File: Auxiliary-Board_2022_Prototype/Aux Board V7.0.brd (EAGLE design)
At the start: 114.3 x 96.6 mm, 56 parts, among them CON11 1X01, CON12 1X01, CON13 1X01, CON14 1X01, CON15 1X01, CON16 1X01, CON17 1X01, CON18 1X01, CON5 1X01, CON8 1X01, IC1 RS232-TTL_MAX232E

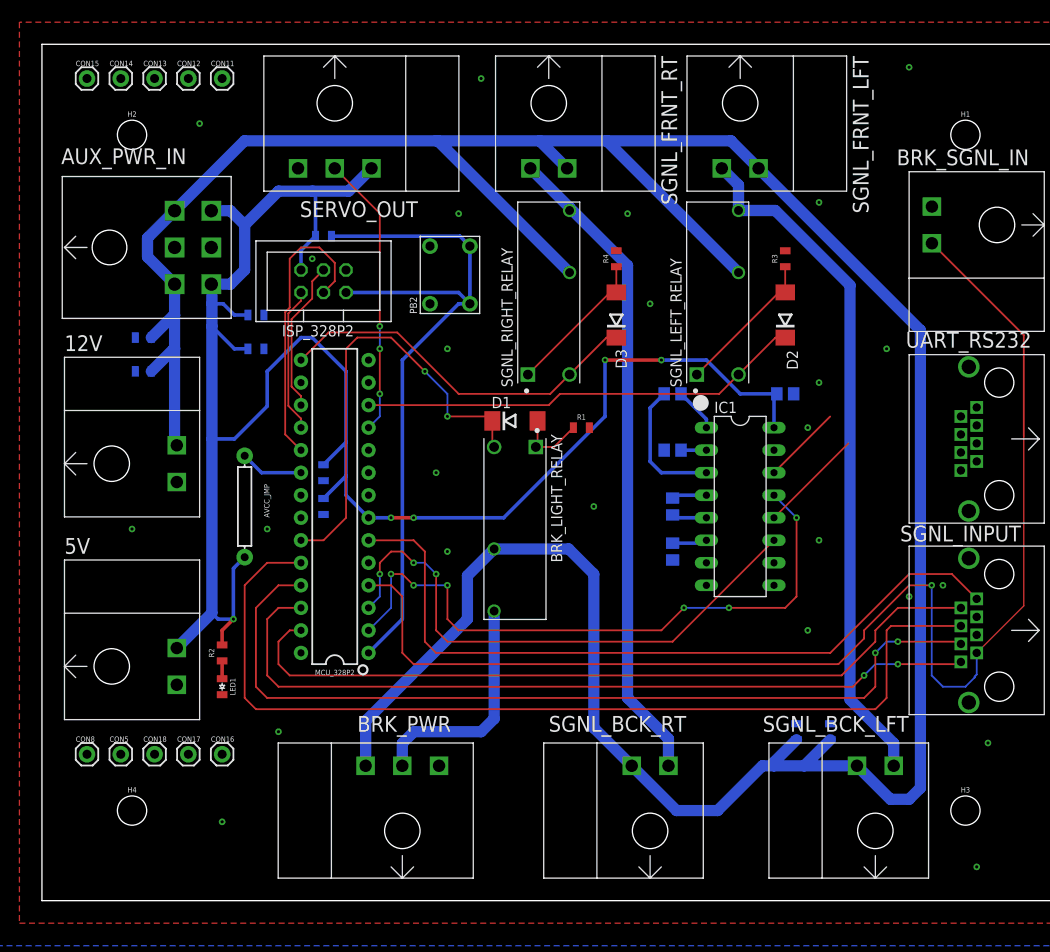
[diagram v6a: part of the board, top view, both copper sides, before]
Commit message: feat: add EcoCar logo and version on board
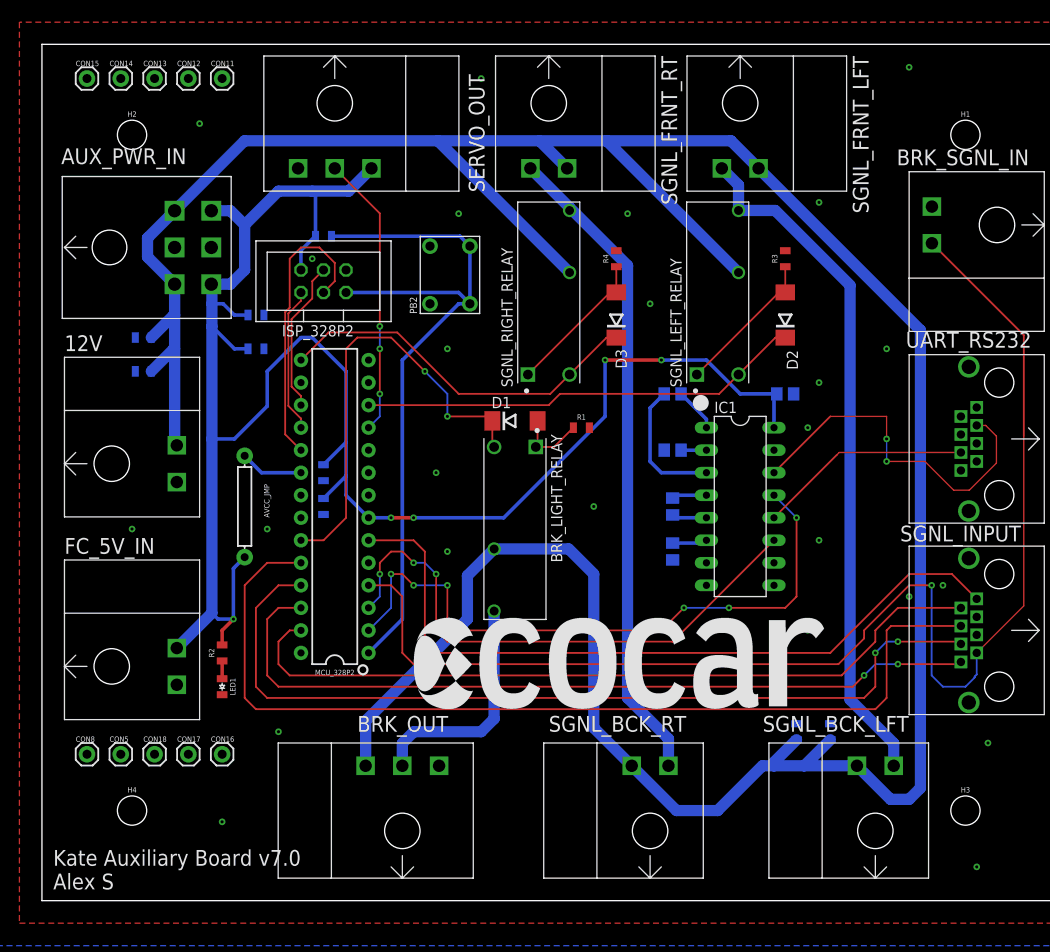
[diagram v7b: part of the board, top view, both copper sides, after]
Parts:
- added U$1: (no value), EcoCar-Miscellaneous:ECOCAR_LOGO_2018
- renumbered 5V to FC_5V_IN, BRK_PWR to BRK_OUT
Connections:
- net RS_RX: now also UART_RS232.6; no longer UART_RS232.3
- net RS_TX: now also UART_RS232.3; no longer UART_RS232.6
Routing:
- net RS_TX: track 8.97 -> 41.2 mm, vias 0 -> 2
- net RS_RX: track 11.9 -> 24.1 mm
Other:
- board text added: "Kate Auxiliary Board v7.0 Alex S"
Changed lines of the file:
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@@
 <wire x1="114.28" y1="101.651" x2="0" y2="101.651" width="0" layer="20"/>
 <wire x1="0" y1="101.651" x2="0" y2="5.08" width="0" layer="20"/>
+<text x="1.27" y="6.35" size="1.778" layer="25">Kate Auxiliary Board v7.0
+Alex S</text>
 </plain>
 <attributes>
@@
 <attribute name="NAME" x="2.54" y="67.056" size="1.778" layer="25"/>
 </element>
-<element name="5V" library="EcoCar-Connectors" package="TE_2-PIN" value="TE_2-PIN" x="2.54" y="31.496" smashed="yes" rot="R270">
+<element name="FC_5V_IN" library="EcoCar-Connectors" package="TE_2-PIN" value="TE_2-PIN" x="2.54" y="31.496" smashed="yes" rot="R270">
 <attribute name="NAME" x="2.54" y="44.196" size="1.778" layer="25"/>
 </element>
@@
 <attribute name="VALUE" x="48.124459375" y="57.6755" size="1.27208125" layer="27" rot="R270"/>
 </element>
-<element name="BRK_PWR" library="EcoCar-Connectors" package="TE_3-PIN" value="TE_3-PIN" x="40.64" y="7.62" smashed="yes">
+<element name="BRK_OUT" library="EcoCar-Connectors" package="TE_3-PIN" value="TE_3-PIN" x="40.64" y="7.62" smashed="yes">
 <attribute name="NAME" x="35.56" y="24.13" size="1.778" layer="25"/>
 </element>
@@
 </element>
 <element name="SERVO_OUT" library="EcoCar-Connectors" package="TE_3-PIN" value="TE_3-PIN" x="33.02" y="100.33" smashed="yes" rot="R180">
-<attribute name="NAME" x="29.083" y="82.169" size="1.778" layer="25"/>
+<attribute name="NAME" x="49.911" y="84.963" size="1.778" layer="25" rot="R90"/>
 </element>
 <element name="SGNL_BCK_LFT" library="EcoCar-Connectors" package="TE_2-PIN" value="TE_2-PIN" x="93.98" y="7.62" smashed="yes">
@@
 <attribute name="VALUE" x="67.476" y="68.48" size="1.27" layer="27" ratio="10" rot="R90"/>
 </element>
+<element name="U$1" library="EcoCar-Miscellaneous" package="ECOCAR_LOGO_2018" value="" x="41.91" y="26.67" smashed="yes"/>
 </elements>
 <signals>
@@
 <contactref element="SGNL_INPUT" pad="9"/>
 <contactref element="SGNL_INPUT" pad="10"/>
-<contactref element="5V" pad="2"/>
+<contactref element="FC_5V_IN" pad="2"/>
 <contactref element="12V" pad="2"/>
-<contactref element="BRK_PWR" pad="3"/>
+<contactref element="BRK_OUT" pad="3"/>
 <contactref element="SERVO_OUT" pad="3"/>
 <contactref element="C1" pad="1"/>
@@
 <contactref element="UART_RS232" pad="4"/>
 <contactref element="UART_RS232" pad="5"/>
-<wire x1="83.82" y1="78.37" x2="100.36" y2="83.35" width="0" layer="19" extent="1-1"/>
-<wire x1="87.63" y1="63.5" x2="83.82" y2="78.37" width="0" layer="19" extent="1-1"/>
-<wire x1="84.77" y1="62.23" x2="87.63" y2="63.5" width="0" layer="19" extent="16-16"/>
-<wire x1="82.55" y1="55.88" x2="84.77" y2="62.23" width="0" layer="19" extent="16-16"/>
-<wire x1="70.17" y1="55.88" x2="82.55" y2="55.88" width="0" layer="19" extent="16-16"/>
-<wire x1="61.733" y1="58.42" x2="70.17" y2="55.88" width="0" layer="19" extent="1-16"/>
-<wire x1="71.12" y1="43.5" x2="70.17" y2="55.88" width="0" layer="19" extent="16-16"/>
-<wire x1="68.58" y1="72.39" x2="61.733" y2="58.42" width="0" layer="19" extent="1-1"/>
-<wire x1="64.77" y1="78.37" x2="68.58" y2="72.39" width="0" layer="19" extent="1-1"/>
-<wire x1="104.52" y1="65.28" x2="87.63" y2="63.5" width="0" layer="19" extent="1-1"/>
-<wire x1="103.63" y1="57.65" x2="104.52" y2="65.28" width="0" layer="19" extent="1-1"/>
-<wire x1="105.41" y1="56.64" x2="103.63" y2="57.65" width="0" layer="19" extent="1-1"/>
-<wire x1="104.52" y1="49.02" x2="105.41" y2="56.64" width="0" layer="19" extent="1-1"/>
-<wire x1="104.52" y1="43.69" x2="104.52" y2="49.02" width="0" layer="19" extent="1-1"/>
-<wire x1="101.6" y1="40.64" x2="104.52" y2="43.69" width="0" layer="19" extent="1-1"/>
-<wire x1="97.79" y1="39.37" x2="101.6" y2="40.64" width="0" layer="19" extent="1-1"/>
-<wire x1="105.41" y1="37.08" x2="101.6" y2="40.64" width="0" layer="19" extent="1-1"/>
-<wire x1="105.41" y1="35.05" x2="105.41" y2="37.08" width="0" layer="19" extent="1-1"/>
-<wire x1="104.52" y1="27.43" x2="105.41" y2="35.05" width="0" layer="19" extent="1-1"/>
-<wire x1="86.36" y1="35.56" x2="97.79" y2="39.37" width="0" layer="19" extent="1-1"/>
-<wire x1="85.09" y1="25.03" x2="86.36" y2="35.56" width="0" layer="19" extent="16-16"/>
-<wire x1="88.9" y1="25.03" x2="85.09" y2="25.03" width="0" layer="19" extent="16-16"/>
-<wire x1="45.72" y1="67.31" x2="61.733" y2="58.42" width="0" layer="19" extent="1-1"/>
-<wire x1="43.76" y1="72.39" x2="45.72" y2="67.31" width="0" layer="19" extent="1-1"/>
-<wire x1="43.76" y1="78.89" x2="43.76" y2="72.39" width="0" layer="19" extent="1-1"/>
-<wire x1="34.29" y1="76.2" x2="43.76" y2="78.89" width="0" layer="19" extent="1-1"/>
-<wire x1="30.48" y1="77.47" x2="34.29" y2="76.2" width="0" layer="19" extent="1-1"/>
-<wire x1="25.03" y1="71.12" x2="30.48" y2="77.47" width="0" layer="19" extent="16-16"/>
-<wire x1="25.03" y1="67.31" x2="25.03" y2="71.12" width="0" layer="19" extent="16-16"/>
-<wire x1="19.1" y1="78.74" x2="25.03" y2="71.12" width="0" layer="19" extent="16-16"/>
-<wire x1="14.96" y1="78.74" x2="19.1" y2="78.74" width="0" layer="19" extent="1-1"/>
-<wire x1="28.88" y1="87.66" x2="30.48" y2="77.47" width="0" layer="19" extent="1-1"/>
-<wire x1="10.53" y1="68.58" x2="14.96" y2="78.74" width="0" layer="19" extent="16-16"/>
-<wire x1="10.53" y1="64.77" x2="10.53" y2="68.58" width="0" layer="19" extent="16-16"/>
-<wire x1="15.21" y1="52.286" x2="10.53" y2="64.77" width="0" layer="19" extent="16-16"/>
-<wire x1="25.4" y1="46.99" x2="15.21" y2="52.286" width="0" layer="19" extent="1-1"/>
-<wire x1="29.21" y1="48.26" x2="25.4" y2="46.99" width="0" layer="19" extent="1-1"/>
-<wire x1="31.75" y1="48.63" x2="29.21" y2="48.26" width="0" layer="19" extent="16-16"/>
-<wire x1="31.75" y1="52.44" x2="31.75" y2="48.63" width="0" layer="19" extent="16-16"/>
-<wire x1="36.83" y1="50.8" x2="31.75" y2="52.44" width="0" layer="19" extent="16-16"/>
-<wire x1="20.32" y1="28.31" x2="25.4" y2="46.99" width="0" layer="19" extent="1-1"/>
-<wire x1="15.21" y1="29.426" x2="20.32" y2="28.31" width="0" layer="19" extent="1-1"/>
-<wire x1="26.67" y1="24.13" x2="20.32" y2="28.31" width="0" layer="19" extent="1-1"/>
-<wire x1="44.78" y1="20.29" x2="26.67" y2="24.13" width="0" layer="19" extent="1-1"/>
 </signal>
 <signal name="12V">
@@
 <contactref element="C7" pad="2"/>
 <contactref element="C5" pad="2"/>
-<contactref element="BRK_PWR" pad="1"/>
+<contactref element="BRK_OUT" pad="1"/>
 <contactref element="AUX_PWR_IN" pad="4"/>
 <contactref element="AUX_PWR_IN" pad="6"/>
@@
 <wire x1="95.69" y1="16.51" x2="91.91" y2="20.29" width="1.27" layer="16"/>
 <wire x1="99.06" y1="69.41" x2="99.06" y2="17.78" width="1.27" layer="16"/>
-<wire x1="22.8474" y1="90.7674" x2="44.45" y2="90.7674" width="1.27" layer="16"/>
+<wire x1="22.8474" y1="90.7674" x2="44.6426" y2="90.7674" width="1.27" layer="16"/>
 <wire x1="44.6426" y1="90.7674" x2="56.1126" y2="90.7674" width="1.27" layer="16"/>
 <wire x1="59.22" y1="87.66" x2="56.1126" y2="90.7674" width="1.27" layer="16"/>
@@
 <wire x1="78.55" y1="75.91" x2="63.6926" y2="90.7674" width="1.27" layer="16"/>
 <wire x1="59.5" y1="75.91" x2="44.6426" y2="90.7674" width="1.27" layer="16"/>
-<wire x1="44.6426" y1="90.7674" x2="44.45" y2="90.7674" width="1.27" layer="16"/>
 </signal>
 <signal name="5V">
-<contactref element="5V" pad="1"/>
+<contactref element="FC_5V_IN" pad="1"/>
 <contactref element="C2" pad="2"/>
 <contactref element="C3" pad="2"/>
@@
 </signal>
 <signal name="BRK_12V">
-<contactref element="BRK_PWR" pad="2"/>
+<contactref element="BRK_OUT" pad="2"/>
 <contactref element="BRK_LIGHT_RELAY" pad="4"/>
 <wire x1="40.64" y1="20.29" x2="40.64" y2="22.83" width="1.27" layer="16"/>
@@
 <contactref element="IC1" pad="14"/>
 <wire x1="82.55" y1="53.34" x2="88.89" y2="59.68" width="0.2032" layer="1"/>
-<contactref element="UART_RS232" pad="6"/>
-<wire x1="88.89" y1="59.68" x2="103.63" y2="55.62" width="0" layer="19" extent="1-1"/>
+<contactref element="UART_RS232" pad="3"/>
+<wire x1="88.89" y1="59.68" x2="88.9" y2="59.69" width="0.1524" layer="1"/>
+<wire x1="88.9" y1="59.69" x2="95.25" y2="59.69" width="0.1524" layer="1"/>
+<wire x1="95.25" y1="59.69" x2="95.25" y2="57.15" width="0.1524" layer="1"/>
+<via x="95.25" y="57.15" extent="1-16" drill="0.35"/>
+<wire x1="95.25" y1="57.15" x2="95.25" y2="54.61" width="0.1524" layer="16"/>
+<via x="95.25" y="54.61" extent="1-16" drill="0.35"/>
+<wire x1="95.25" y1="54.61" x2="99.5687125" y2="54.61" width="0.1524" layer="1"/>
+<wire x1="107.6326" y1="57.4586875" x2="106.4212875" y2="58.67" width="0.1524" layer="1"/>
+<wire x1="105.41" y1="58.67" x2="106.4212875" y2="58.67" width="0.1524" layer="1"/>
+<wire x1="99.5687125" y1="54.61" x2="102.8113125" y2="51.3674" width="0.1524" layer="1"/>
+<wire x1="102.8113125" y1="51.3674" x2="104.5736875" y2="51.3674" width="0.1524" layer="1"/>
+<wire x1="104.5736875" y1="51.3674" x2="107.6326" y2="54.4263125" width="0.1524" layer="1"/>
+<wire x1="107.6326" y1="54.4263125" x2="107.6326" y2="57.4586875" width="0.1524" layer="1"/>
 </signal>
 <signal name="RS_RX">
 <contactref element="IC1" pad="12"/>
-<wire x1="82.55" y1="48.26" x2="90.93" y2="56.64" width="0.2032" layer="1"/>
-<contactref element="UART_RS232" pad="3"/>
-<wire x1="90.93" y1="56.64" x2="105.41" y2="58.67" width="0" layer="19" extent="1-1"/>
+<wire x1="82.55" y1="48.26" x2="89.66" y2="55.37" width="0.2032" layer="1"/>
+<contactref element="UART_RS232" pad="6"/>
+<wire x1="89.66" y1="55.37" x2="89.91" y2="55.62" width="0.1524" layer="1"/>
+<wire x1="89.91" y1="55.62" x2="103.63" y2="55.62" width="0.1524" layer="1"/>
 </signal>
 <signal name="RX">
@@
 </drawing>
 <compatibility>
+<note version="6.3" minversion="6.2.2" severity="warning">
+Since Version 6.2.2 text objects can contain more than one line,
+which will not be processed correctly with this version.
+</note>
 <note version="8.2" severity="warning">
 Since Version 8.2, EAGLE supports online libraries. The ids
